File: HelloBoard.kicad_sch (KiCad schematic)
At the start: 0 parts

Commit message: Added Power, I2C, BOOT0, NRST, HSE, USB, SWD, TempSensor
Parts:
- added C1, C14, C2, C3, C4, C9: 100n, symbol Device:C
- added C10, C11: 10p, symbol Device:C
- added C12, C5: 10u, symbol Device:C
- added C13: 22u, symbol Device:C
- added C6: 10n, symbol Device:C
- added C7, C8: 1u, symbol Device:C
- added D1: RED, symbol Device:LED
- added FB1: 120R, symbol Device:FerriteBead
- added J1: USB_B_Micro, symbol Connector:USB_B_Micro
- added J2, J3: Conn_01x04_Pin, symbol Connector:Conn_01x04_Pin
- added R1: 10K, symbol Device:R
- added R2, R4: 2K2, symbol Device:R
- added R3: 1K5, symbol Device:R
- added SW1: SW_Push, symbol Switch:SW_Push
- added U1: STM32F103C8T6, Package_QFP:LQFP-48_7x7mm_P0.5mm, symbol MCU_ST_STM32F1:STM32F103C8Tx
- added U2: AMS1117-3.3, Package_TO_SOT_SMD:SOT-223-3_TabPin2, symbol Regulator_Linear:AMS1117-3.3
- added U3: TMP235A2DCKR, TMP235A2DCKR:SOT65P210X110-5N, symbol TMP235A2DCKR:TMP235A2DCKR
- added Y1: 16MHz, symbol Device:Crystal_GND24
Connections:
- new net: C14.1, U3.4 (VCC)
- new net +3.3V: C1.1, C13.1, C2.1, C3.1, C4.1, C5.1, C8.1, D1.2 (A), FB1.2, J2.1 (Pin_1), J3.1 (Pin_1), R2.1, R4.1, U1.1 (VBAT), U1.24 (VDD), U1.36 (VDD), U1.48 (VDD), U2.2 (VO)
- new net +3.3VA: C6.1, C7.1, FB1.1, U1.9 (VDDA)
- new net BOOT0: R1.2, U1.44 (BOOT0)
- new net GND: C1.2, C10.2, C11.2, C12.2, C13.2, C14.2, C2.2, C3.2, C4.2, C5.2, C6.2, C7.2, C8.2, C9.2, J1.5 (GND), J2.4 (Pin_4), J3.4 (Pin_4), R1.1, R3.1, SW1.1, U1.23 (VSS), U1.35 (VSS), U1.47 (VSS), U1.8 (VSSA), U2.1 (GND), U3.1 (GND1), U3.2 (VSS), U3.5 (GND2), Y1.2 (G), Y1.4 (G)
- new net HSE_IN: C11.1, U1.5 (PD0), Y1.1
- new net HSE_OUT: C10.1, U1.6 (PD1), Y1.3
- new net I2C_SCL: J3.2 (Pin_2), R2.2, U1.42 (PB6)
- new net I2C_SDA: J3.3 (Pin_3), R4.2, U1.43 (PB7)
- new net NRST: C9.1, SW1.2, U1.7 (NRST)
- new net PWR_LED_K: D1.1 (K), R3.2
- new net SWCLK: J2.3 (Pin_3), U1.37 (PA14)
- new net SWDIO: J2.2 (Pin_2), U1.34 (PA13)
- new net Temp_OUT: U1.10 (PA0), U3.3 (OUT)
- new net VBUS: C12.1, J1.1 (VBUS), U2.3 (VI)
- no-connect marks 0 -> 4
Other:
- note added: "100nF decoupling capacitor per VDD pin and a single 10uF bulk decoupling capacitor (See AN2586 document by STMicroelectronics)"
- note added: "Analog Temp Sensor Circuit"
- note added: "Boot Pin Configuration (RM008 page 60 shows different boot modes) (10K resistor value taken from example circuit in AN4488)"
- note added: "External Crystal Oscillator (HSE) circuit Asssume a stray capacitance value of 5pF Use X322516MMB4SI for Oscillator 10pF Load Capacitance according to manufacturer (Cload - Cstray) * 2 = CL1 & CL2 value = 10pF (Refer to AN2867 document by ST for formula page 12)"
- note added: "I2C Circuit"
- note added: "Power Circuit See AMS1117-3.3 Datasheet for capacitor values"
- note added: "Reset Circuit (See STM32F103C8T6 Datasheet Page 67)"
- note added: "SWD Header"
- note added: "USB Circuit (See AN4879 by STMicroelectronics for the Pull-Up resistor value) (note 2 in table 4 page 3)"
- company: (none) -> University Of Jordan
- title: (none) -> HelloBoard !

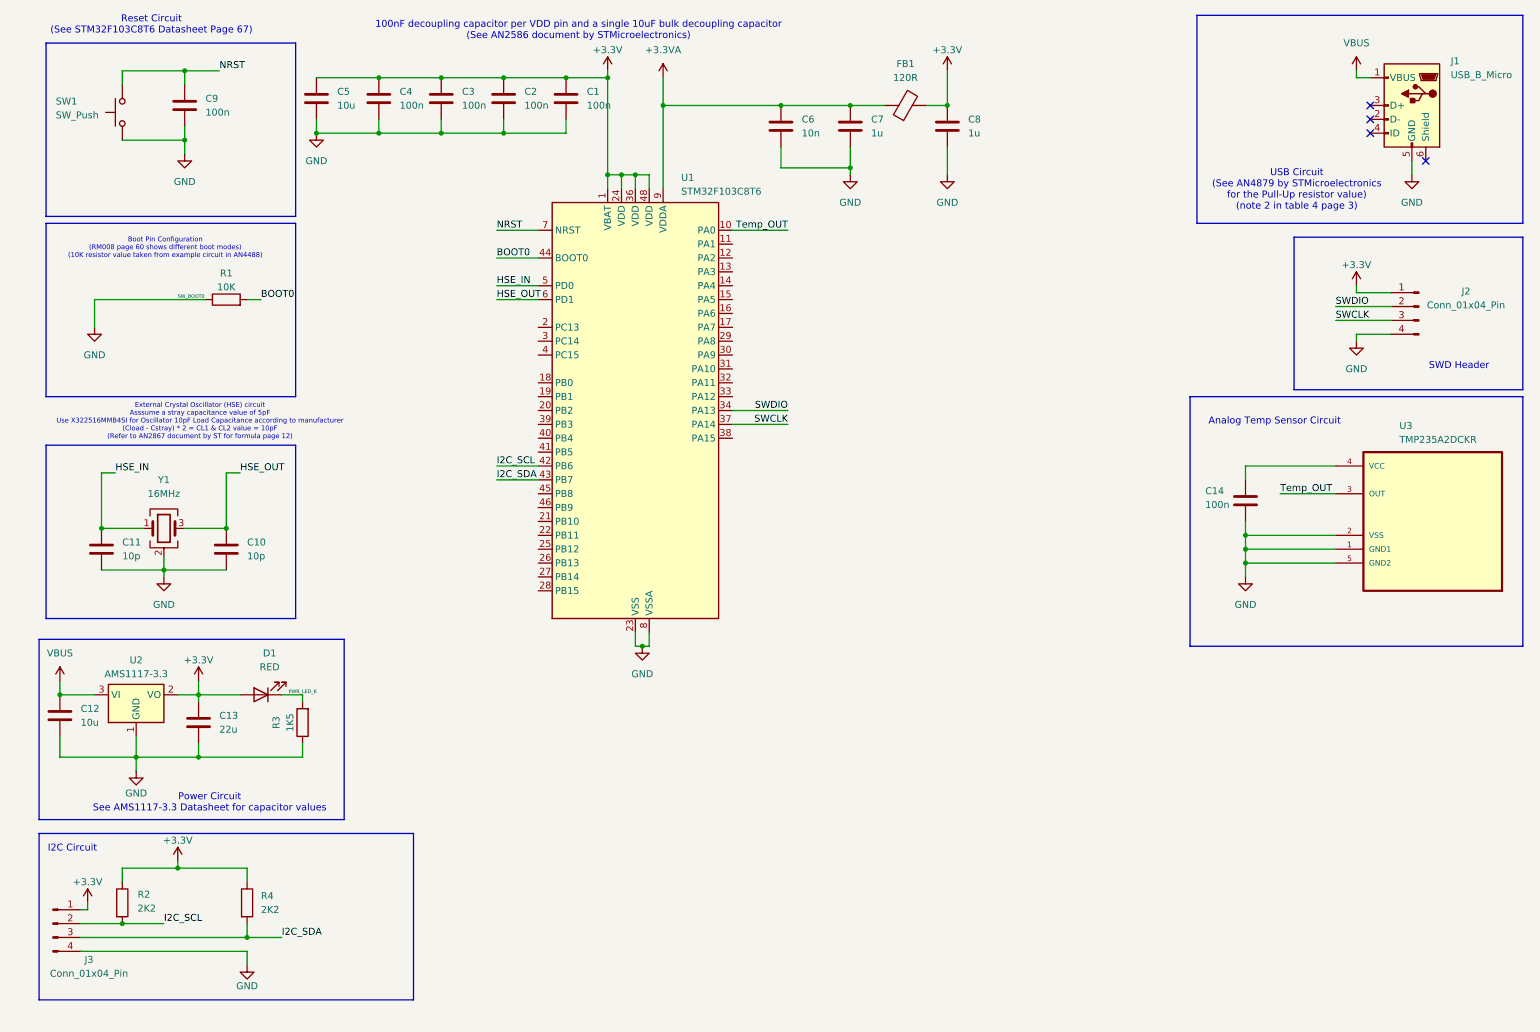
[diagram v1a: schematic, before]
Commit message: added user push button, user LED, 4 digit 7 segment ?
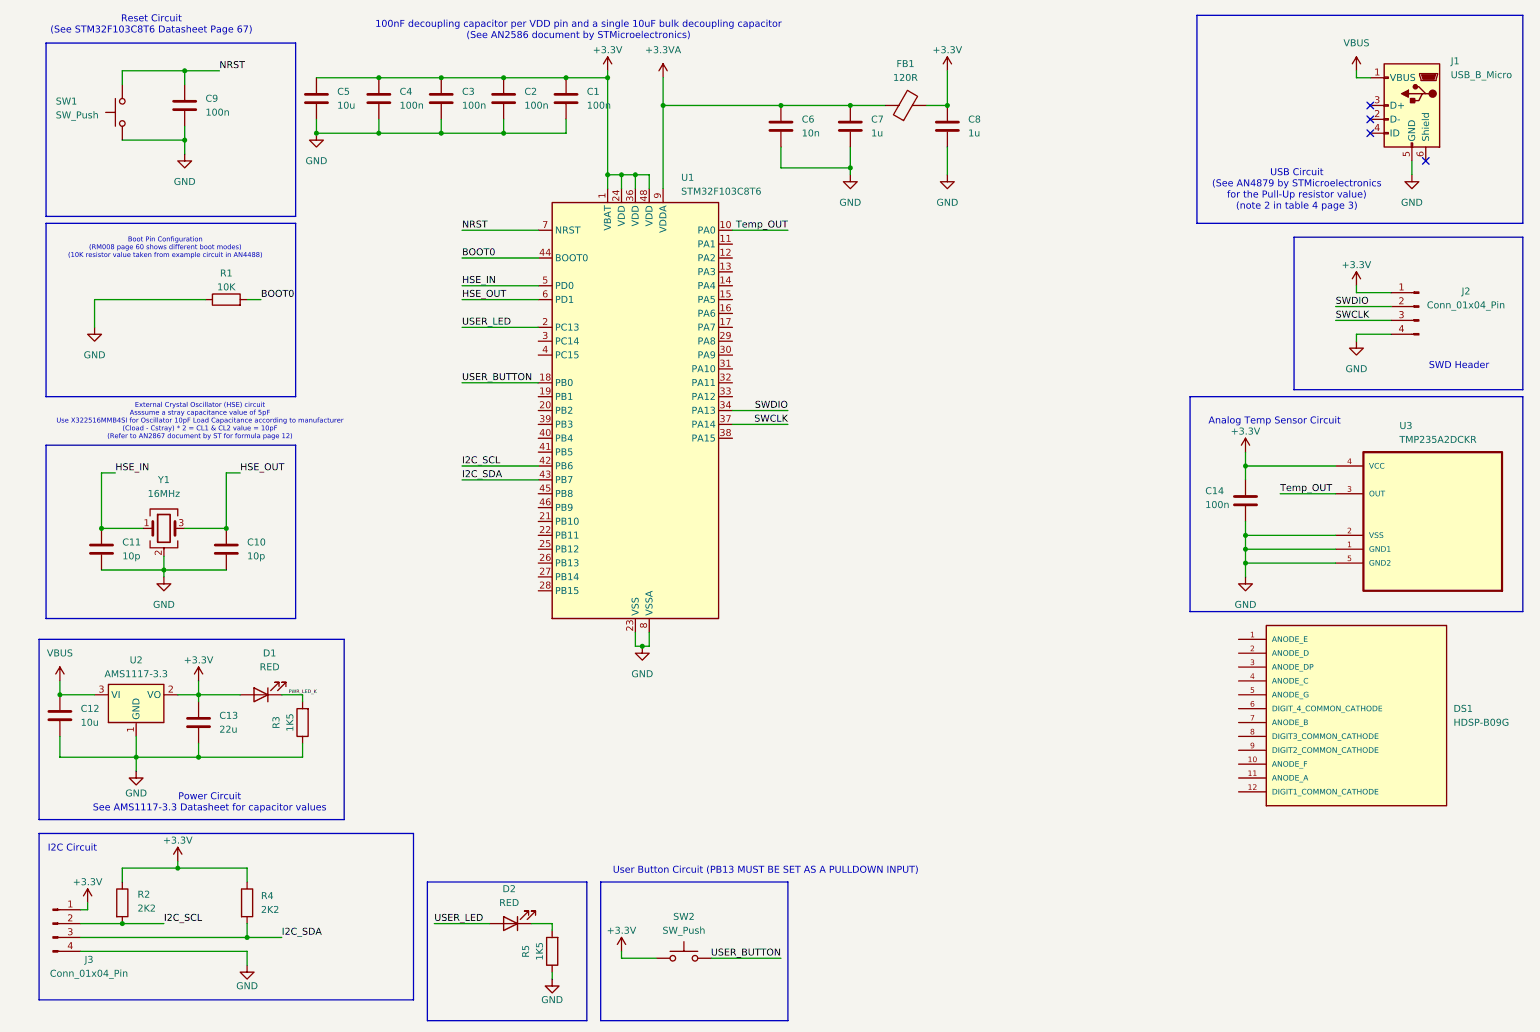
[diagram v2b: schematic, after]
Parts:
- added D2: RED, symbol Device:LED
- added DS1: HDSP-B09G, HDSP-B09G:AVAGO_HDSP-B09G, symbol HDSP-B09G:HDSP-B09G
- added R5: 1K5, symbol Device:R
- added SW2: SW_Push, symbol Switch:SW_Push
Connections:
- net +3.3V: now also C14.1, U3.4 (VCC), SW2.1
- net GND: now also R5.1
- net USER_BUTTON: now reaches U1.18 (PB0)
- net USER_BUTTON: now also SW2.2
- net USER_LED: now reaches U1.2 (PC13)
- net USER_LED: now also D2.2 (A)
- new net: D2.1 (K), R5.2
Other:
- note added: "User Button Circuit (PB13 MUST BE SET AS A PULLDOWN INPUT)"

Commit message: added 16x2 LCD
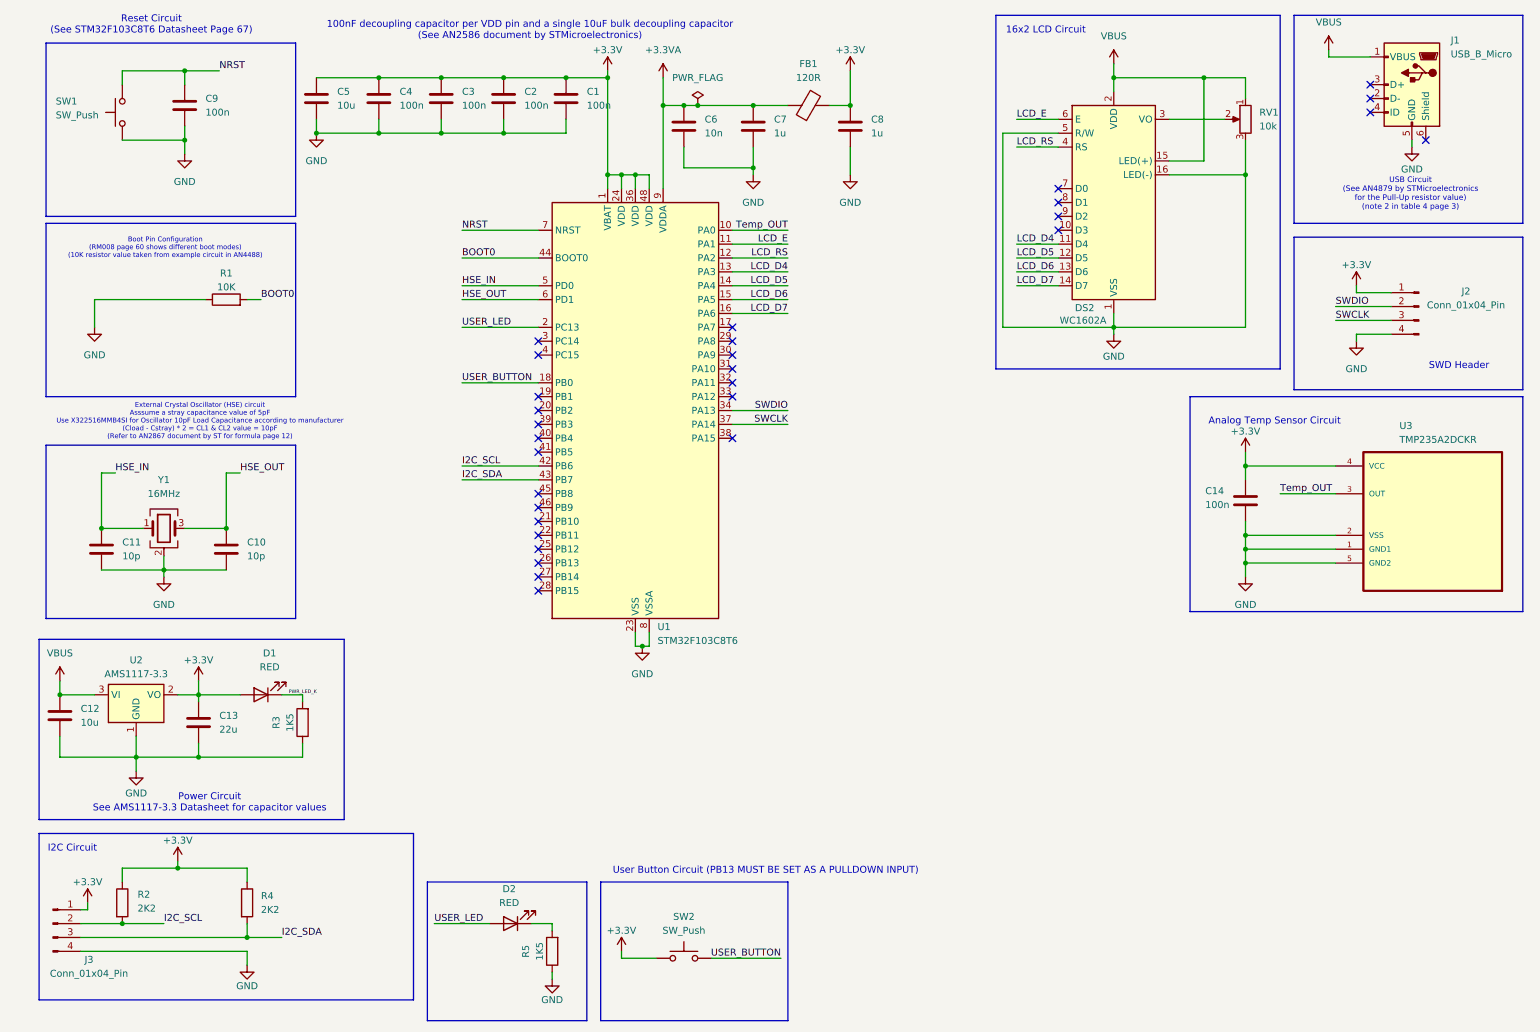
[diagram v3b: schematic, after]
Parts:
- removed DS1: HDSP-B09G, HDSP-B09G:AVAGO_HDSP-B09G, symbol HDSP-B09G:HDSP-B09G
- added DS2: WC1602A, Display:WC1602A, symbol Display_Character:WC1602A
- added RV1: 10k, symbol Device:R_Potentiometer
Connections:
- net GND: now also DS2.1 (VSS), DS2.16 (LED(-)), DS2.5 (R/W), RV1.3
- net VBUS: now also DS2.15 (LED(+)), DS2.2 (VDD), RV1.1
- net LCD_E: now reaches U1.11 (PA1)
- net LCD_E: now also DS2.6 (E)
- net LCD_RS: now reaches U1.12 (PA2)
- net LCD_RS: now also DS2.4 (RS)
- net LCD_D4: now reaches U1.13 (PA3)
- net LCD_D4: now also DS2.11 (D4)
- net LCD_D5: now reaches U1.14 (PA4)
- net LCD_D5: now also DS2.12 (D5)
- net LCD_D6: now reaches U1.15 (PA5)
- net LCD_D6: now also DS2.13 (D6)
- net LCD_D7: now reaches U1.16 (PA6)
- net LCD_D7: now also DS2.14 (D7)
- new net: DS2.3 (VO), RV1.2
- no-connect marks 4 -> 30
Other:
- note added: "16x2 LCD Circuit"
- moved on the sheet: C6, C7, C8, FB1, J1

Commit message: Finished Schematic (for now)
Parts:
- added J4: Conn_02x08_Top_Bottom, Connector_PinHeader_1.00mm:PinHeader_2x08_P1.00mm_Vertical, symbol Connector_Generic:Conn_02x08_Top_Bottom
- added U4: ADXL343, Package_LGA:LGA-14_3x5mm_P0.8mm_LayoutBorder1x6y, symbol Sensor_Motion:ADXL343
- added U5: DA56-11CGKWA, Display_7Segment:DA56-11CGKWA, symbol Display_Character:DA56-11CGKWA
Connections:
- net +3.3V: now also J4.15 (Pin_15), U4.1 (Vdd_I/O), U4.12 (SDO/ADDR), U4.6 (Vs), U4.7 (~{CS})
- net GND: now also J4.16 (Pin_16), U4.2 (GND), U4.4 (GND), U4.5 (GND)
- net I2C_SCL: now also U4.14 (SCL/SCLK)
- net I2C_SDA: now also U4.13 (SDA/SDI/SDIO)
- net VBUS: now also J4.14 (Pin_14)
- net PA_7: now reaches U1.17 (PA7)
- net PA_7: now also J4.8 (Pin_8)
- net PB_1: now reaches U1.19 (PB1)
- net PB_1: now also J4.3 (Pin_3)
- net PB_2: now reaches U1.20 (PB2)
- net PB_2: now also J4.4 (Pin_4)
- net 7SEG_C: now reaches U1.21 (PB10)
- net 7SEG_C: now also U5.3 (DIG1_C), U5.8 (DIG2_C)
- net 7SEG_D: now reaches U1.22 (PB11)
- net 7SEG_D: now also U5.2 (DIG1_D), U5.6 (DIG2_D)
- net 7SEG_E: now reaches U1.25 (PB12)
- net 7SEG_E: now also U5.1 (DIG1_E), U5.5 (DIG2_E)
- net 7SEG_F: now reaches U1.26 (PB13)
- net 7SEG_F: now also U5.12 (DIG2_F), U5.18 (DIG1_F)
- net 7SEG_G: now reaches U1.27 (PB14)
- net 7SEG_G: now also U5.17 (DIG1_G), U5.7 (DIG2_G)
- net 7SEG_D1_CA: now reaches U1.28 (PB15)
- net 7SEG_D1_CA: now also U5.14 (DIG1_CA)
- net PA_8: now reaches U1.29 (PA8)
- net PA_8: now also J4.9 (Pin_9)
- net PC_14: now reaches U1.3 (PC14)
- net PC_14: now also J4.1 (Pin_1)
- net PA_9: now reaches U1.30 (PA9)
- net PA_9: now also J4.10 (Pin_10)
- net PA_10: now reaches U1.31 (PA10)
- net PA_10: now also J4.11 (Pin_11)
- net PA_11: now reaches U1.32 (PA11)
- net PA_11: now also J4.12 (Pin_12)
- net PA_12: now reaches U1.33 (PA12)
- net PA_12: now also J4.13 (Pin_13)
- net 7SEG_D2_CA: now reaches U1.38 (PA15)
- net 7SEG_D2_CA: now also U5.13 (DIG2_CA)
- net PB_3: now reaches U1.39 (PB3)
- net PB_3: now also J4.5 (Pin_5)
- net PC_15: now reaches U1.4 (PC15)
- net PC_15: now also J4.2 (Pin_2)
- net PB_4: now reaches U1.40 (PB4)
- net PB_4: now also J4.6 (Pin_6)
- net PB_5: now reaches U1.41 (PB5)
- net PB_5: now also J4.7 (Pin_7)
- net 7SEG_A: now reaches U1.45 (PB8)
- net 7SEG_A: now also U5.11 (DIG2_A), U5.16 (DIG1_A)
- net 7SEG_B: now reaches U1.46 (PB9)
- net 7SEG_B: now also U5.10 (DIG2_B), U5.15 (DIG1_B)
- no-connect marks 30 -> 14
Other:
- note added: "2 Digit 7 Segment Display Circuit"
- note added: "Accelerometer/Gyrscope Circuit"
- note added: "GPIO Pin Header"
- note added: "User Button Circuit (PB0 MUST BE SET AS A PULLDOWN INPUT)"
- note removed: "User Button Circuit (PB13 MUST BE SET AS A PULLDOWN INPUT)"
